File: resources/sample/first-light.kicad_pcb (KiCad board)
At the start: 2 copper layers, 40 x 28 mm, 2 parts

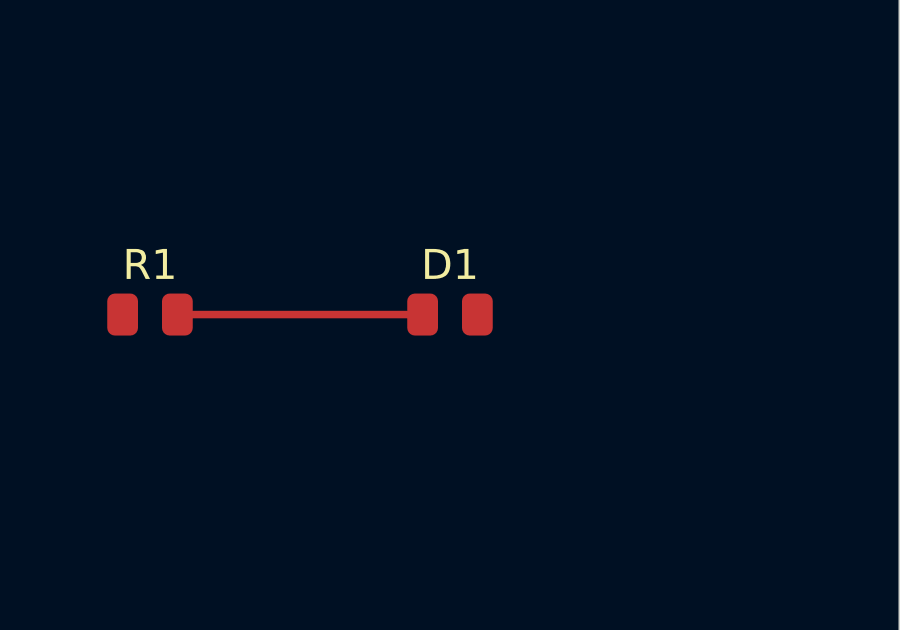
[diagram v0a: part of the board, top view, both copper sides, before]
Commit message: test(e2e): First Light spec + fix reversed LED on the demo board
e2e/first-light.spec.ts drives the full flow against the built app:
open demo -> Energize -> poll window.__circsimLedGlow until D1 glows
(>0.05, cross-checked against <html data-led-glow-max>) -> lower the
supply to 2.5 V -> assert the glow dims. All waits poll the glow
instrumentation; no fixed sim sleeps. 4/4 passing runs, ~4.4 s each.

Writing the spec exposed a shipped bug: first-light.kicad_pcb had D1
wired pad1=LEDA / pad2=GND, but the bundled library pinMap for LED_*
footprints follows the KiCad convention (pad 1 = cathode), so the deck
put the diode in reverse (~5 V reverse bias, 64 uA leakage, dark LED).
Swapped the pad nets and rotated D1 180 deg so the anode pad sits on the
LEDA trace end. Measured after fix: D1 glow 0.804 @ 5 V -> 0.374 @ 2.5 V
(~9.4 mA vs ~2 mA through 330 ohm).

Known siblings (fixed next): blinker-555.kicad_pcb has the same
reversed LED; the coach polarity diagnosis assumes pad1=anode.

Co-Authored-By: Claude Fable 5 <noreply@anthropic.com>
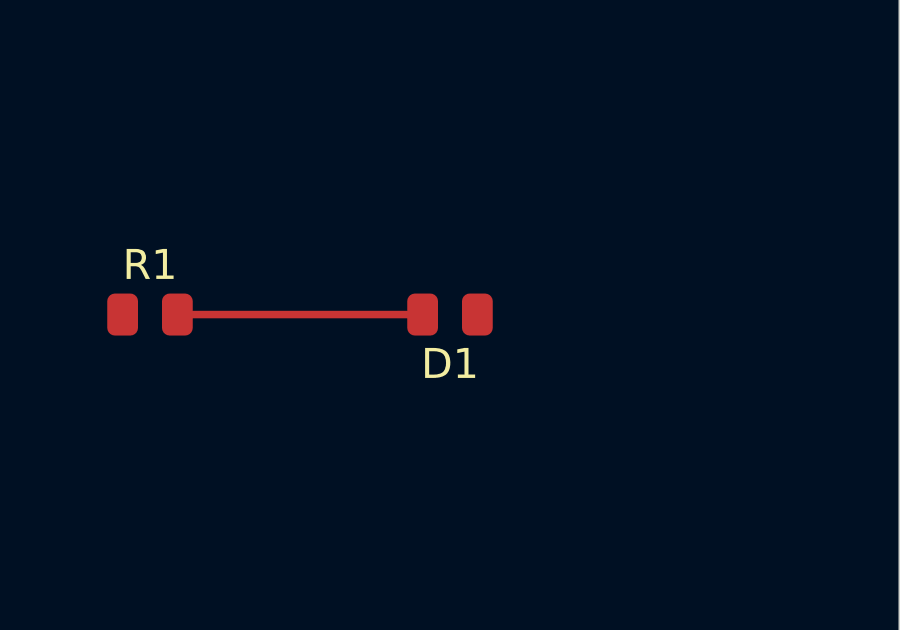
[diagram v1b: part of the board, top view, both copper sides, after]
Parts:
- turned D1 to 180 degrees
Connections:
- D1 pad 1: LEDA -> GND
- D1 pad 2: GND -> LEDA
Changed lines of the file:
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@@
   )
   (footprint "LED_SMD:LED_0805_2012Metric" (layer "F.Cu")
-    (at 25 12)
+    (at 25 12 180)
     (fp_text reference "D1" (at 0 -1.65) (layer "F.SilkS")
       (effects (font (size 1 1) (thickness 0.15))))
     (fp_text value "LED" (at 0 1.65) (layer "F.Fab")
       (effects (font (size 1 1) (thickness 0.15))))
-    (pad "1" smd roundrect (at -0.9125 0) (size 1.025 1.4)
+    (pad "1" smd roundrect (at -0.9125 0 180) (size 1.025 1.4)
+      (layers "F.Cu" "F.Paste" "F.Mask") (roundrect_rratio 0.25) (net 3 "GND"))
+    (pad "2" smd roundrect (at 0.9125 0 180) (size 1.025 1.4)
       (layers "F.Cu" "F.Paste" "F.Mask") (roundrect_rratio 0.25) (net 2 "LEDA"))
-    (pad "2" smd roundrect (at 0.9125 0) (size 1.025 1.4)
-      (layers "F.Cu" "F.Paste" "F.Mask") (roundrect_rratio 0.25) (net 3 "GND"))
   )
   (segment (start 15.9125 12) (end 24.0875 12) (width 0.25) (layer "F.Cu") (net 2 "LEDA"))
